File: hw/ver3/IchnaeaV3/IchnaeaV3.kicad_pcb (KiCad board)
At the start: 4 copper layers, 100 x 100 mm, 279 parts, among them J1 Terminal Block, J2 Terminal Block, J5 FanConnector, Q1 BSS138, Q10 HYG053N10NS1C2, Q11 HYG053N10NS1C2, Q12 BSS138, Q13 BSS138, Q14 BSS138, Q15 BSS84, Q16 BSS138, Q17 HYG053N10NS1C2, Q18 HYG053N10NS1C2, Q2 HYG053N10NS1C2, Q20 HYG053N10NS1C2, Q21 HYG053N10NS1C2, Q22 HYG053N10NS1C2, Q23 HYG053N10NS1C2, Q24 HYG053N10NS1C2, Q25 HYG053N10NS1C2, Q26 HYG053N10NS1C2, Q27 HYG053N10NS1C2, Q3 HYG053N10NS1C2, Q4 HYG053N10NS1C2, Q5 HYG053N10NS1C2, Q6 HYG053N10NS1C2, Q7 HYG053N10NS1C2, Q8 HYG053N10NS1C2, Q9 HYG053N10NS1C2, U1 INA180A4, U10 HIP2210, U11 HIP2210, U16 ADS1220xPW, U17 74HC4051PW, U18 74HC4051PW, U19 INA180A4, U2 LTC7871, U20 TPSI3050, U3 AP66200FVBW-13, U4 LM1117MP-5.0, U6 HIP2210, U7 HIP2210, U8 HIP2210, U9 HIP2210

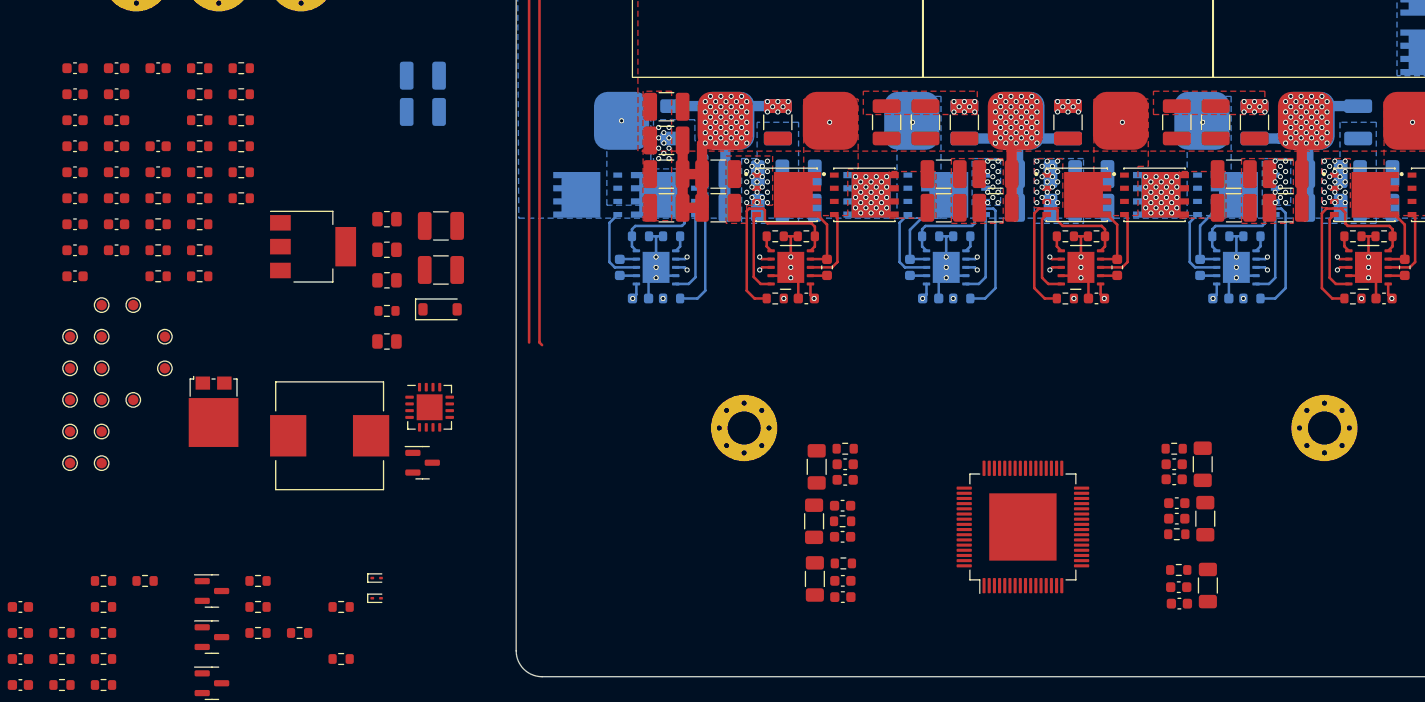
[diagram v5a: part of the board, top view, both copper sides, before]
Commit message: Begin routing switching controller signals
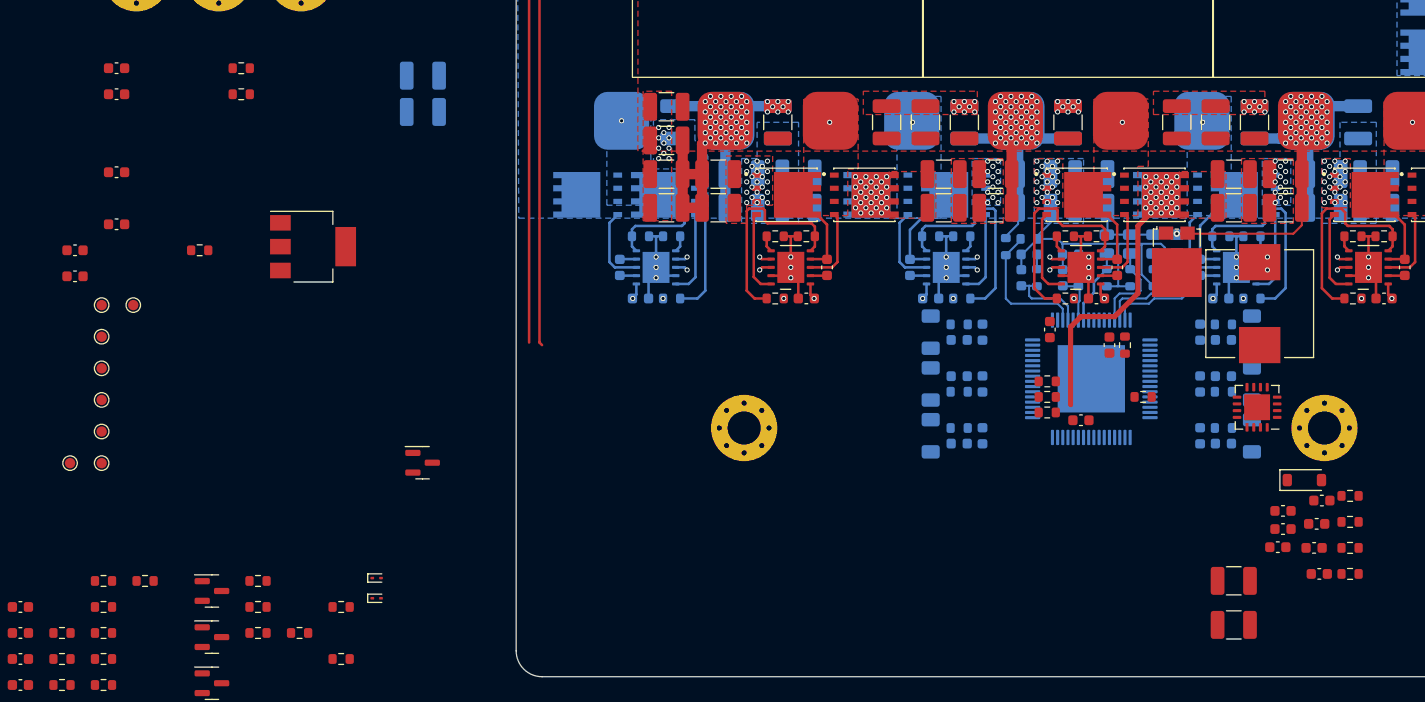
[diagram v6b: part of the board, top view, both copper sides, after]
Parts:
- removed TP18, TP22, TP23, TP4, TP5, TP6, TP7: TestPoint, TestPoint:TestPoint_Pad_D1.0mm
- C2, C3, C31, C32, C4, C42, C43, C5, C53, C54, C64, C65, C75, C76, C86, C87, R10, R12, R13, R14, R15, R16, R18, R21, R33, R34, R38, R39, R43, R44, R48, R49, R53, R54, R6, R7, R72, R73, R8, R9, U2: moved to B.Cu
- moved C18 121.6 mm to (172.5, 145.1)
- moved C22 120.1 mm to (172.2, 140.2)
- moved C20 118.8 mm to (172.8, 138.0)
- moved C15 118.7 mm to (169.0, 139.0)
- moved C16 118.5 mm to (169.0, 140.8)
- moved C26 117.3 mm to (172.0, 142.6)
- moved C25 114.8 mm to (168.5, 142.5)
- moved R26 113.0 mm to (175.5, 137.6)
- moved R27 113.0 mm to (175.5, 140.1)
- moved R28 113.0 mm to (175.5, 142.6)
- moved R29 113.0 mm to (175.5, 145.1)
- moved C7 100.8 mm to (152.2, 123.0), turned to -90 degrees
- moved C6 100.0 mm to (149.5, 130.2)
- moved C2 97.4 mm to (147.8, 116.5), turned to 90 degrees
- moved C4 96.9 mm to (148.5, 114.2), turned to 180 degrees
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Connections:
- R18 pad 1: HT -> VIN
- R8 pad 1: HT -> VIN
- R9 pad 1: HT -> VIN
- U2 pad 17: /PowerStage/Phase1/SNSA+ -> /PowerStage/Phase3/SNSA+
- U2 pad 19: /PowerStage/Phase1/SNSD+ -> /PowerStage/Phase3/SNSD+
- U2 pad 23: /PowerStage/Phase3/SNSA+ -> /PowerStage/Phase1/SNSA+
- U2 pad 25: /PowerStage/Phase3/SNSD+ -> /PowerStage/Phase1/SNSD+
- U2 pad 29: /PowerStage/Phase1/PWM -> /PowerStage/Phase3/PWM
- U2 pad 32: /PowerStage/Phase3/PWM -> /PowerStage/Phase1/PWM
- U2 pad 33: /PowerStage/Phase4/PWM -> /PowerStage/Phase6/PWM
- U2 pad 36: /PowerStage/Phase6/PWM -> /PowerStage/Phase4/PWM
- U2 pad 56: /PowerStage/Phase4/SNSD+ -> /PowerStage/Phase6/SNSD+
- U2 pad 58: /PowerStage/Phase4/SNSA+ -> /PowerStage/Phase6/SNSA+
- U2 pad 62: /PowerStage/Phase6/SNSD+ -> /PowerStage/Phase4/SNSD+
- U2 pad 64: /PowerStage/Phase6/SNSA+ -> /PowerStage/Phase4/SNSA+
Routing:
- net GND: track 78.5 -> 116.1 mm
- net VIN: track 0.00 -> 30.7 mm
- net VLOW: track 226.3 -> 243.8 mm, vias 183 -> 184
- net LTC_VFB_LOW: track 0.00 -> 13.3 mm
- net LTC_OV_LOW: track 0.00 -> 12.1 mm
- net LTC_UV_HIGH: track 0.00 -> 10.5 mm
- net LTC_OV_HIGH: track 0.00 -> 8.90 mm
- net LTC_ITH_LOW: track 0.00 -> 8.00 mm
- net LTC_FB_HIGH: track 0.00 -> 7.36 mm
- net LTC_ITH_HIGH: track 0.00 -> 4.89 mm
- net Net-(C5-Pad1): track 0.00 -> 1.44 mm
- net Net-(C4-Pad1): track 0.00 -> 1.44 mm
- added copper zone on In1.Cu, net +12V
